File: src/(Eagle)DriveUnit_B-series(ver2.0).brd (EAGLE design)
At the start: 65.7 x 51 mm, 67 parts, among them IC1 A3921, SW1 TVAF06-A020B-R, SW2 TVAF06-A020B-R, SW3 THAF01-NC-R, SW4 SS-12D00G3

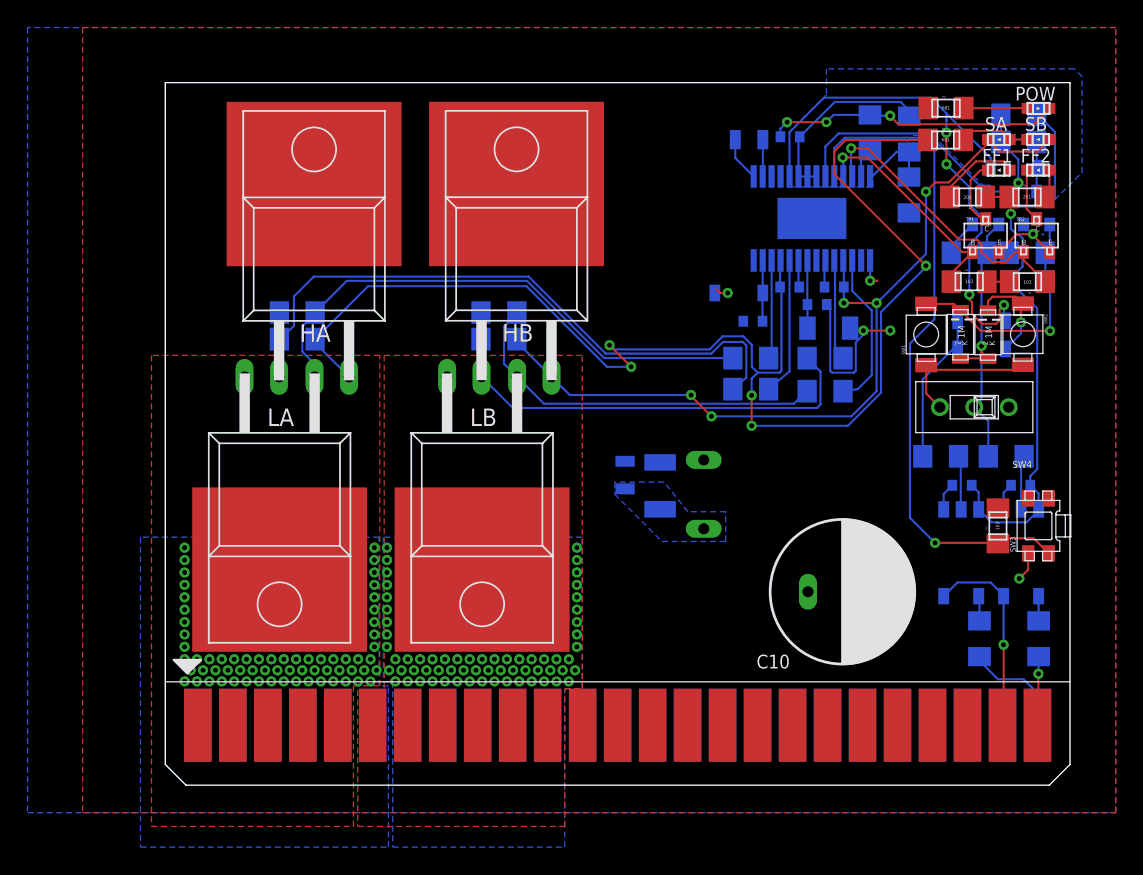
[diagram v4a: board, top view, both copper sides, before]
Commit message: モタドラ配線完全終了_KiCad移行前
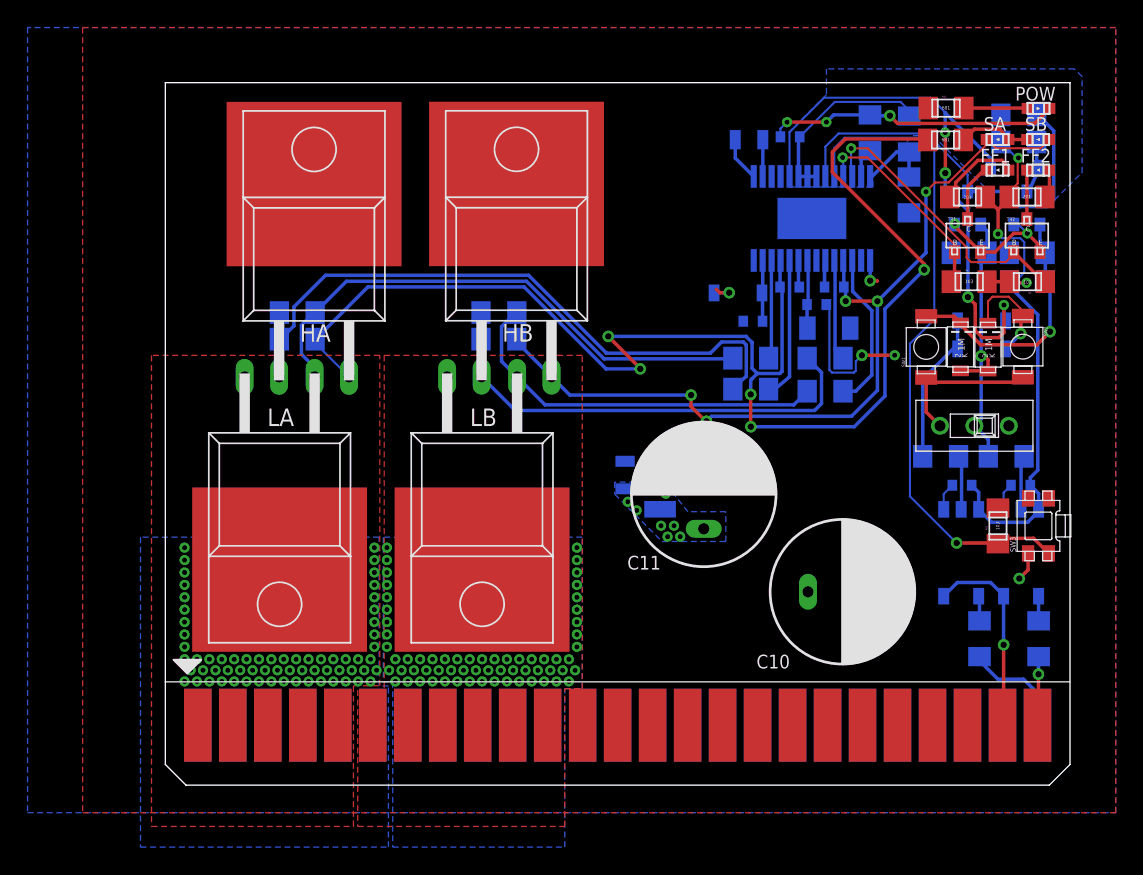
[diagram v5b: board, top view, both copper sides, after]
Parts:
- moved SW4 1.35 mm to (58.7, 26.1)
- moved TR3 1.31 mm to (57.3, 40.7)
- moved TR1 1.31 mm to (59.2, 38.7)
- moved D4 0.90 mm to (57.7, 33.6)
- moved D5 0.90 mm to (59.7, 33.5)
- moved SW1 0.90 mm to (55.2, 29.6)
- moved SW2 0.90 mm to (62.3, 34.1)
- moved TR4 0.71 mm to (61.6, 40.7)
- moved TR2 0.71 mm to (63.5, 38.7)
- moved LED1 0.09 mm to (59.6, 46.9)
- moved LED4 0.09 mm to (59.6, 44.6)
- moved D1 0.06 mm to (43.3, 35.7)
- flipped C11 to the top
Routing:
- net V5: track 56.0 -> 60.6 mm, vias 2 -> 3
- net N$13: track 43.4 -> 45.8 mm
- net SA: track 99.4 -> 101.5 mm
- net FF1: track 16.5 -> 14.9 mm
- net DIR: track 42.3 -> 43.8 mm
- net N$17: track 17.8 -> 19.0 mm
- net GND: track 58.5 -> 59.5 mm, vias 7 -> 8
- net RESET: track 49.1 -> 48.2 mm
- net N$9: track 6.22 -> 7.07 mm
- net GHB: track 6.62 -> 7.42 mm
- net N$5: track 5.17 -> 4.37 mm
- net PWM: track 28.4 -> 29.0 mm
- net N$20: track 7.38 -> 7.97 mm
- net VCC: track 3.87 -> 4.15 mm, vias 2 -> 11

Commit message: 回路ミスってた(嘘だろ...)_KiCad以降前
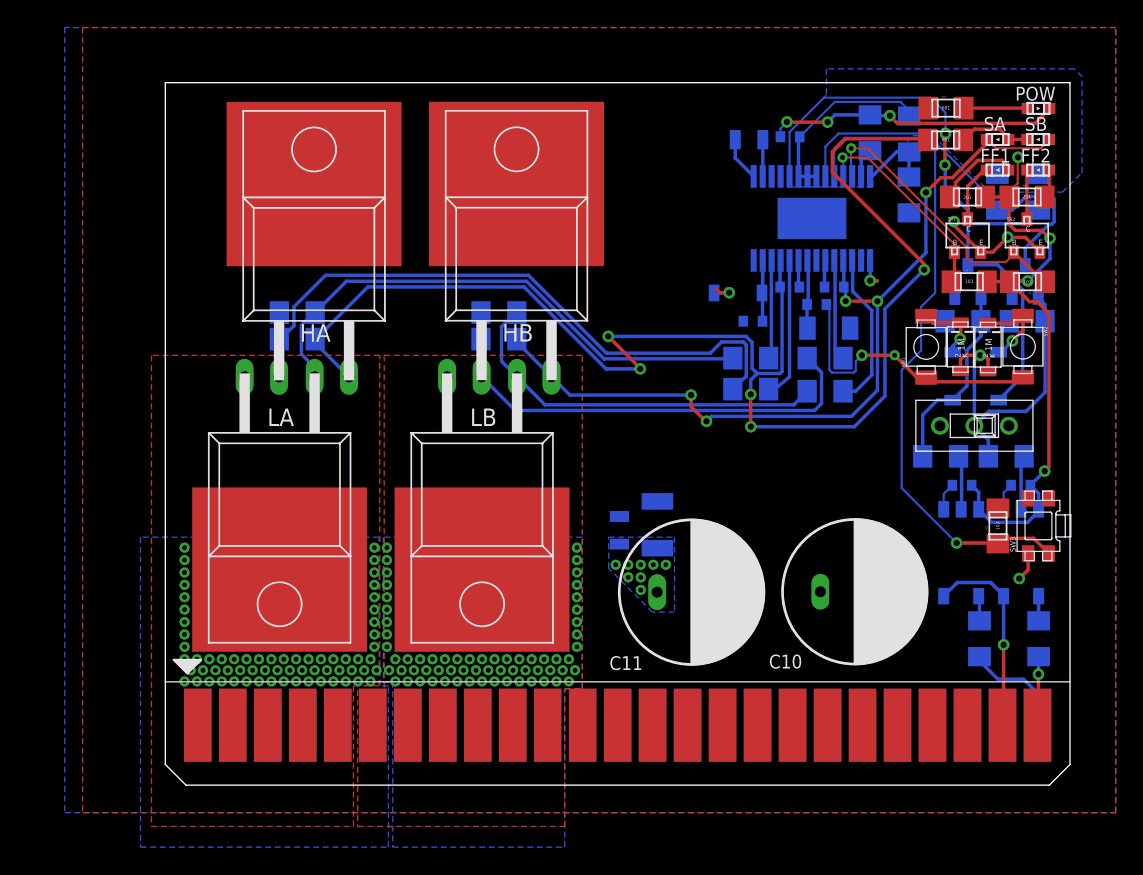
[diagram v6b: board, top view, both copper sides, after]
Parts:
- removed D6: GS1010FL, GS1010FL:GS1010FL
- removed R23: RG2012, RG2012:RG2012
- moved D3 13.4 mm to (60.5, 31.4), turned to 270 degrees
- moved R17 7.81 mm to (63.4, 44.4), turned to 270 degrees
- moved C11 7.15 mm to (38.2, 14.0), turned to 90 degrees
- moved TR4 6.84 mm to (57.3, 35.4)
- moved R24 6.82 mm to (59.2, 33.7)
- moved TR3 6.78 mm to (61.5, 35.4)
- moved R25 6.51 mm to (63.9, 33.7)
- moved D2 4.47 mm to (57.2, 31.4), turned to 270 degrees
- moved R6 4.32 mm to (60.4, 44.4), turned to 270 degrees
- moved C13 4.03 mm to (33.0, 18.5)
- moved C12 2.84 mm to (35.7, 18.9)
- moved C10 0.90 mm to (50.1, 14.0)
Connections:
- removed net N$17: D4.C, R17.LEFT, R24.LEFT, SW1.RIGHT, TR4.B
- removed net N$27: D2.A, D6.A, R1.LEFT
- new net N$16: D2.A, R1.LEFT, R24.LEFT, TR4.B
- net DIR: now also D3.A, R17.RIGHT, TR4.C; no longer D2.C, D3.C
- net N$12: now also D2.C, D4.C, SW1.RIGHT; no longer D3.A, R23.LEFT, TR4.C
- net N$20: now also D3.C; no longer D6.C
- net V5: now also R17.LEFT; no longer R17.RIGHT, R23.RIGHT
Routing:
- net N$17: track 19.0 -> 0.00 mm, vias 1 -> 0
- net N$16: track 0.00 -> 13.9 mm
- net N$27: track 11.2 -> 0.00 mm
- net LAP: track 21.3 -> 25.2 mm
- net DIR: track 43.8 -> 46.8 mm, vias 4 -> 2
- net V5: track 60.6 -> 57.7 mm, vias 3 -> 4
- net GND: track 59.5 -> 56.8 mm
- net N$12: track 3.88 -> 5.07 mm, vias 0 -> 1
- net PWM: track 29.0 -> 28.0 mm
- net N$20: track 7.97 -> 7.23 mm
- net RESET: track 48.2 -> 48.7 mm
- net VCC: vias 11 -> 10
